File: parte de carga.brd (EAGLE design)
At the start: 74.6 x 121.9 mm, 36 parts, among them IC1 MCP73831T-2ACI_OT, IC10 741G3157DBVR, IC15 LMV321AIDCKR, IC16 LMV321AIDCKR, IC2 ESP32-S3-WROOM-1-N16R2, IC5 LMV321AIDCKR, IC7 AD8226ARZ, IC9 LP38692MP-3.3_NOPB, J1 USB3500-30-A-KIT, J3 SJ-3523-SMT-TR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

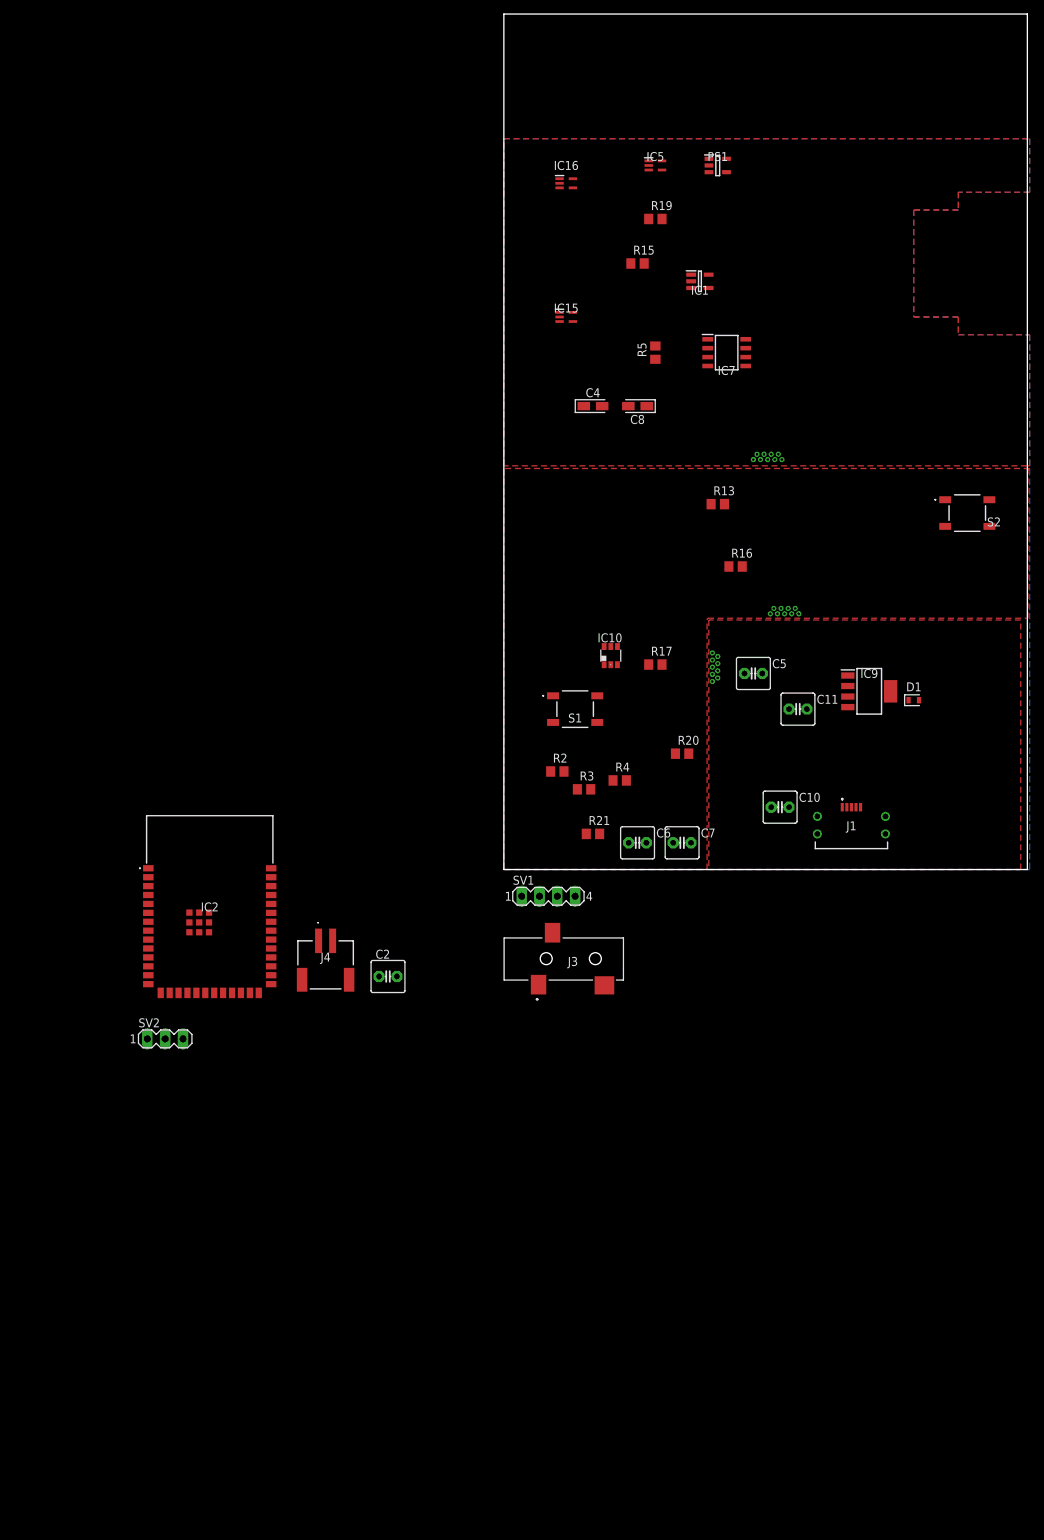
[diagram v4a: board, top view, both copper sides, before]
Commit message: Corregir huellas capacitores, organice esp32 y Amp Op
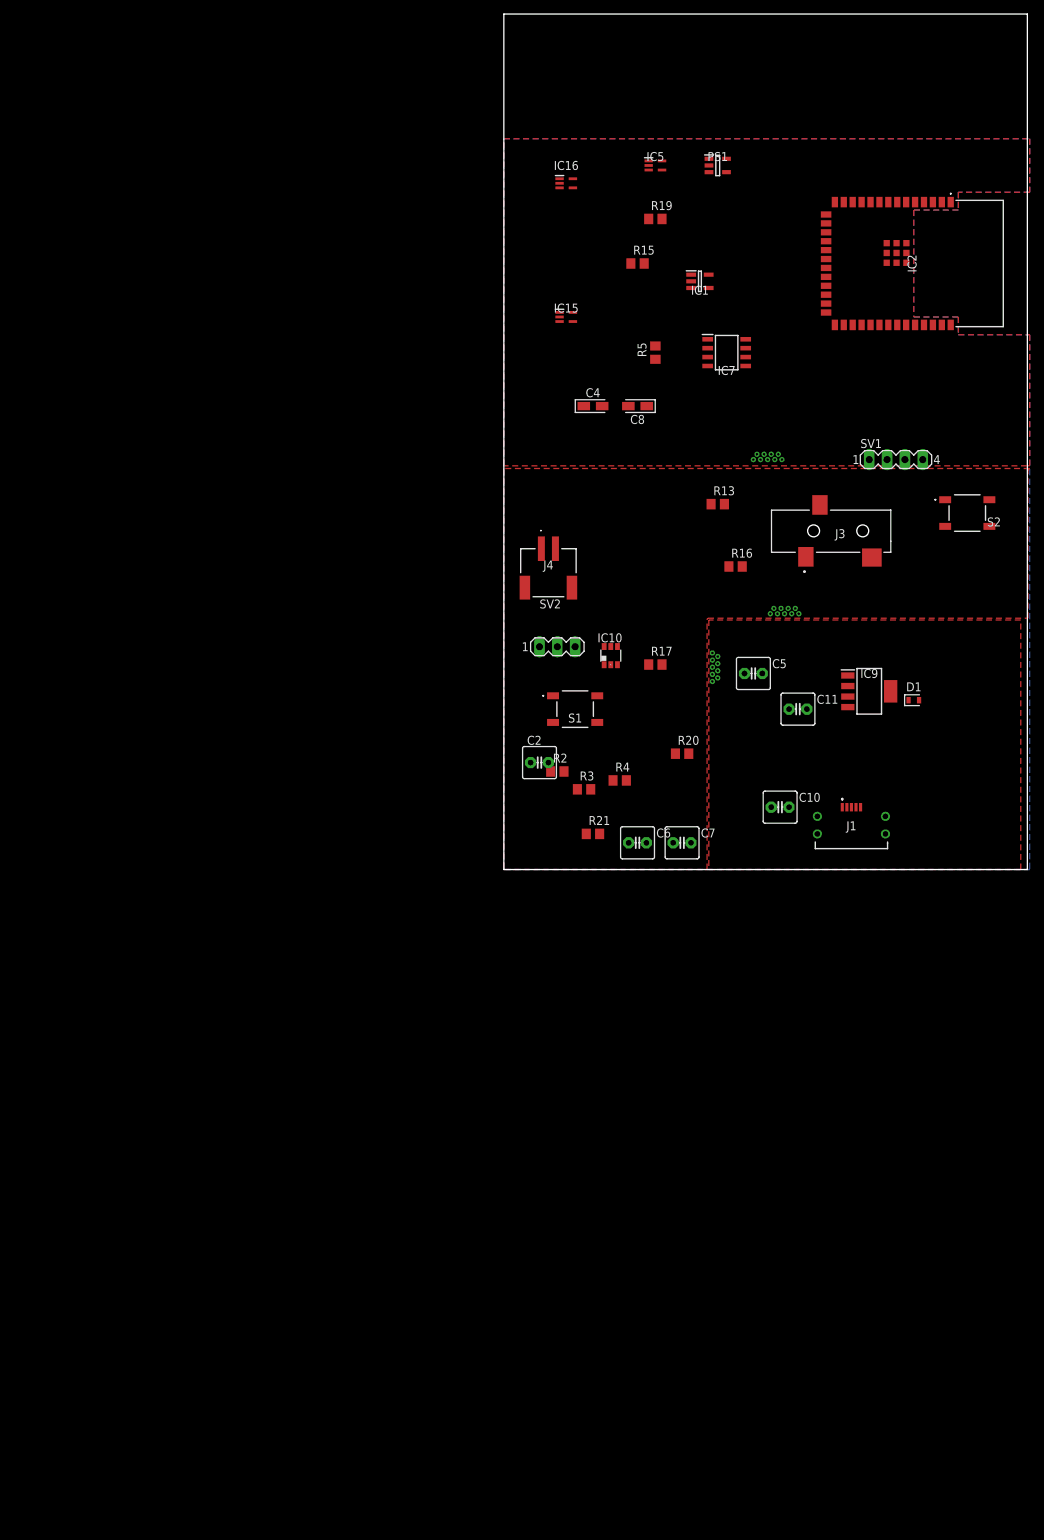
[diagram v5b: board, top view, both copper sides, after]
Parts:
- moved IC2 135.7 mm to (58.4, 88.9), turned to 270 degrees
- moved SV1 79.5 mm to (55.9, 61.0)
- moved SV2 79.0 mm to (7.62, 34.3)
- moved J3 71.9 mm to (40.6, 50.8)
- moved J4 64.3 mm to (6.35, 48.3)
- moved C2 37.4 mm to (5.08, 17.8)
